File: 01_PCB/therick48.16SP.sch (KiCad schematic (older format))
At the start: 181 parts, among them J1 TYPE-C-31-M12_13, J2 AVR-ISP-6_mod, K1 KEYSW, K10 KEYSW, K11 KEYSW, K12 KEYSW, K13 KEYSW, K14 KEYSW, K15 KEYSW, K16 KEYSW, K17 KEYSW, K18 KEYSW, K19 KEYSW, K2 KEYSW, K20 KEYSW, K21 KEYSW, K22 KEYSW, K23 KEYSW, K24 KEYSW, K25 KEYSW, K26 KEYSW, K27 KEYSW, K28 KEYSW, K29 KEYSW, K3 KEYSW, K30 KEYSW, K31 KEYSW, K32 KEYSW, K33 KEYSW, K34 KEYSW, K35 KEYSW, K36 KEYSW, K37 KEYSW, K38 KEYSW, K39 KEYSW, K4 KEYSW, K40 KEYSW, K41 KEYSW, K42 KEYSW, K43 KEYSW, K44 KEYSW, K45 KEYSW, K46 KEYSW, K47 KEYSW, K48 KEYSW, K49 KEYSW, K5 KEYSW, K50 KEYSW, K51 KEYSW, K52 KEYSW, K53 KEYSW, K54 KEYSW, K55 KEYSW, K56 KEYSW, K57 KEYSW, K58 KEYSW, K59 KEYSW, K6 KEYSW, K60 KEYSW, K61 KEYSW, K62 KEYSW, K63 KEYSW, K64 KEYSW, K7 KEYSW, K8 KEYSW, K9 KEYSW, SW1 SW_PUSH, SW2 Rotary_Encoder_Switch, U1 ATMEGA32U4, U10 HOLE, U11 HOLE, U2 HOLE, U3 USBLC6-2SC6, U4 HOLE, U5 HOLE, U6 HOLE, U7 HOLE, U8 HOLE, U9 HOLE, Y1 16MHz

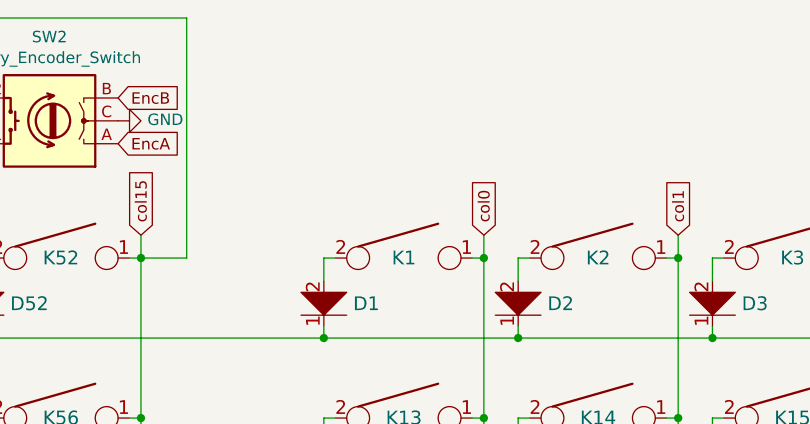
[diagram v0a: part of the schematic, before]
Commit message: Added encoder
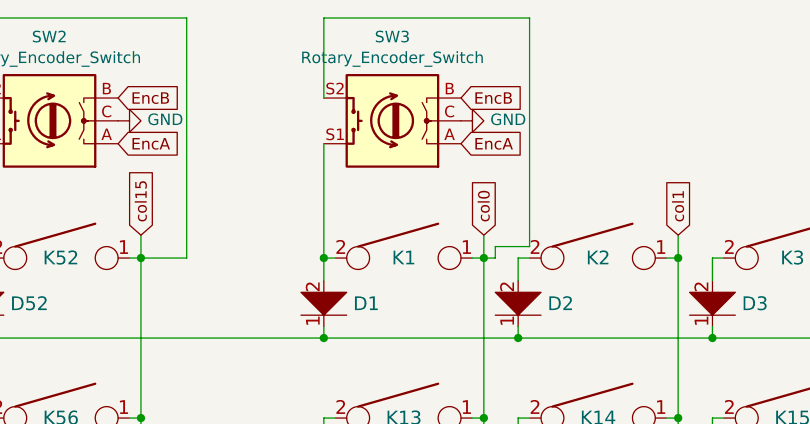
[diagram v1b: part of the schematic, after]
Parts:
- added SW3: Rotary_Encoder_Switch, Keebio-Parts:RotaryEncoder_EC11, symbol Device:Rotary_Encoder_Switch
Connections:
- net EncA: now also SW3.A
- net EncB: now also SW3.B
- net GND: now also SW3.C
- net col0: now also SW3.S2
- net at D1.2, K1.2: now also SW3.S1
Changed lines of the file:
@@
 Wire Notes Line
 	11400 7650 13100 7650
+$Comp
+L Device:Rotary_Encoder_Switch SW3
+U 1 1 5EFCABC9
+P 5850 1350
+F 0 "SW3" H 5850 983 50  0000 C CNN
+F 1 "Rotary_Encoder_Switch" H 5850 1074 50  0000 C CNN
+F 2 "Keebio-Parts:RotaryEncoder_EC11" H 5700 1510 50  0001 C CNN
+F 3 "~" H 5850 1610 50  0001 C CNN
+	1    5850 1350
+	-1   0    0    1
+$EndComp
+Text GLabel 6150 1250 2    50   Input ~ 0
+EncB
+Text GLabel 6150 1450 2    50   Input ~ 0
+EncA
+$Comp
+L power:GND #PWR0129
+U 1 1 5EFCABD1
+P 6150 1350
+F 0 "#PWR0129" H 6150 1100 50  0001 C CNN
+F 1 "GND" V 6155 1222 50  0000 R CNN
+F 2 "" H 6150 1350 50  0001 C CNN
+F 3 "" H 6150 1350 50  0001 C CNN
+	1    6150 1350
+	0    -1   -1   0
+$EndComp
+Wire Wire Line
+	5550 1950 5550 1450
+Connection ~ 5550 1950
+Wire Wire Line
+	5550 1250 5550 900
+Wire Wire Line
+	5550 900  6450 900
+Wire Wire Line
+	6450 900  6450 1900
+Wire Wire Line
+	6450 1900 6300 1900
+Wire Wire Line
+	6300 1900 6300 1950
+Wire Wire Line
+	6300 1950 6250 1950
 $EndSCHEMATC

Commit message: Update
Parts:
- removed U8: HOLE, Artwork:THERICK, symbol lets_split-cache:HOLE
- added SW4, SW5, SW6, SW7, SW8, SW9: Rotary_Encoder_Switch, Keebio-Parts:RotaryEncoder_EC11, symbol Device:Rotary_Encoder_Switch
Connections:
- net EncA: now also SW4.A, SW5.A, SW8.A
- net EncB: now also SW4.B, SW5.B, SW8.B
- net GND: now also SW4.C, SW5.C, SW6.C, SW7.C, SW8.C, SW9.C
- net col0: now also SW5.S2
- net col11: now also SW6.S2, SW7.S2
- net col15: now also SW4.S2
- net col5: now also SW8.S2
- net col6: now also SW9.S2
- net at D12.2, K12.2: now also SW7.S1
- net at D48.2, K48.2: now also SW6.S1
- net at D43.2, K43.2: now also SW9.S1
- net at D42.2, K42.2: now also SW8.S1
- net at D37.2, K37.2: now also SW5.S1
- net EncD: now reaches U1.18 (PD0/INT0)
- net EncD: now also SW6.B, SW7.B, SW9.B
- net EncC: now reaches U1.19 (PD1/INT1)
- net EncC: now also SW6.A, SW7.A, SW9.A
- net at D64.2, K64.2: now also SW4.S1
- no-connect marks 6 -> 4
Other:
- note removed: "THERICK"
- moved on the sheet: C1, C2, C3, C4, C5, C6, CX1, CX2, F1, H1, H10, H11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
